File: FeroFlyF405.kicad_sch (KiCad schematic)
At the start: 4 parts

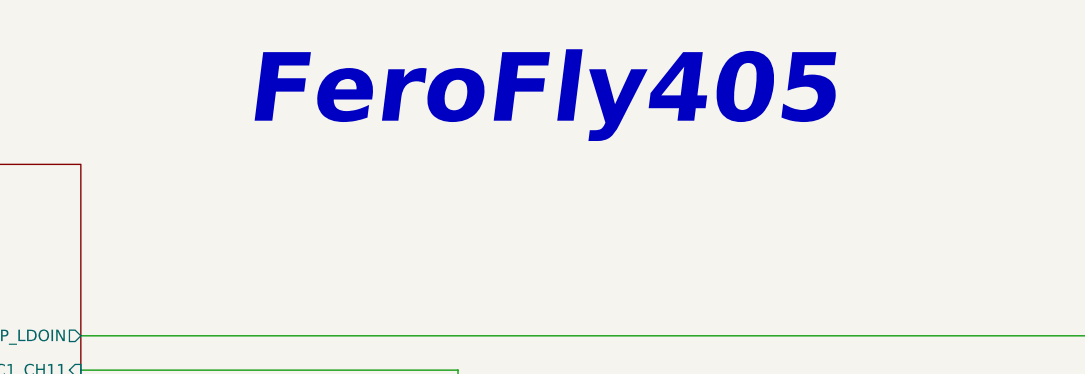
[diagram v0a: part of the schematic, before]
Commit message: refactor: change name from FeroFly405 to FeroFlyF405
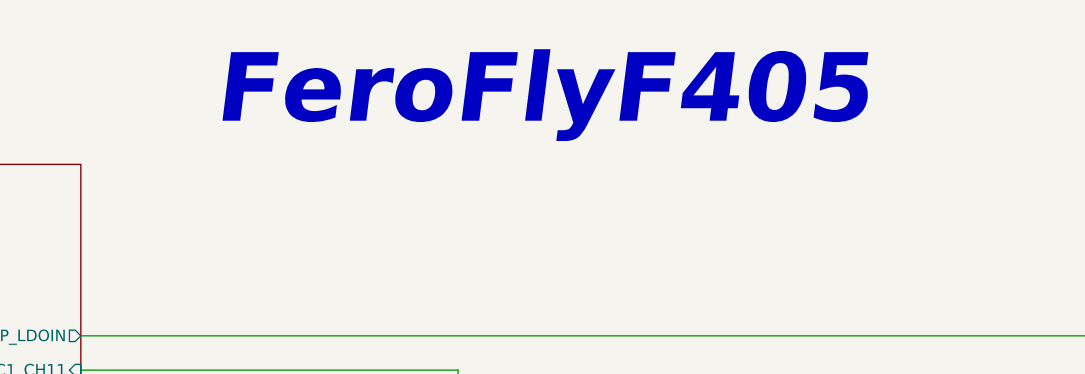
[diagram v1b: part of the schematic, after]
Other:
- note added: "FeroFlyF405"
- note removed: "FeroFly405"
- title: FeroFly405 -> FeroFlyF405
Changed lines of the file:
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@@
 	(paper "A4")
 	(title_block
-		(title "FeroFly405")
+		(title "FeroFlyF405")
 		(date "2026-07-22")
 		(rev "1")
-		(comment 3 "GitHub: https://github.com/Ozonised/FeroFly405")
+		(comment 3 "GitHub: https://github.com/Ozonised/FeroFlyF405")
 		(comment 4 "Designed by: Farhan Khan")
 	)
@@
 		)
 	)
-	(text "FeroFly405"
+	(text "FeroFlyF405"
 		(exclude_from_sim no)
 		(at 149.098 29.972 0)
@@
 		)
 		(instances
-			(project "FeroFly"
+			(project "FeroFlyF405"
 				(path "/8fea5468-8d8d-4bdb-afc0-e65b62c92669"
 					(reference "H103")
@@
 		)
 		(instances
-			(project "FeroFly"
+			(project "FeroFlyF405"
 				(path "/8fea5468-8d8d-4bdb-afc0-e65b62c92669"
 					(reference "H101")
@@
 		)
 		(instances
-			(project "FeroFly"
+			(project "FeroFlyF405"
 				(path "/8fea5468-8d8d-4bdb-afc0-e65b62c92669"
 					(reference "H104")
@@
 		)
 		(instances
-			(project "FeroFly"
+			(project "FeroFlyF405"
 				(path "/8fea5468-8d8d-4bdb-afc0-e65b62c92669"
 					(reference "H102")
@@
 		)
 		(instances
-			(project "FeroFly"
+			(project "FeroFlyF405"
 				(path "/8fea5468-8d8d-4bdb-afc0-e65b62c92669"
 					(page "4")
@@
 		)
 		(instances
-			(project "FeroFly"
+			(project "FeroFlyF405"
 				(path "/8fea5468-8d8d-4bdb-afc0-e65b62c92669"
 					(page "3")
@@
 		)
 		(instances
-			(project "FeroFly"
+			(project "FeroFlyF405"
 				(path "/8fea5468-8d8d-4bdb-afc0-e65b62c92669"
 					(page "2")
@@
 		)
 		(instances
-			(project "FeroFly"
+			(project "FeroFlyF405"
 				(path "/8fea5468-8d8d-4bdb-afc0-e65b62c92669"
 					(page "7")

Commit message: refactor(schematic): assign net classes and fix USB net label assingment
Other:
- sheet MCU ports: added SPI1_CS, SPI1_MISO, SPI1_MOSI, SPI1_SCK; removed D_SPI1_CS, D_SPI1_MISO, D_SPI1_MOSI, D_SPI1_SCK
- sheet Peripherals ports: added SPI1_CS, SPI1_MISO, SPI1_MOSI, SPI1_SCK; removed D_SPI1_CS, D_SPI1_MISO, D_SPI1_MOSI, D_SPI1_SCK
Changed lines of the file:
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@@
 			)
 		)
-		(pin "D_SPI1_CS" output
+		(pin "SPI1_CS" output
 			(at 99.06 110.49 0)
 			(effects
@@
 			)
 		)
-		(pin "D_SPI1_MISO" input
+		(pin "SPI1_MISO" input
 			(at 99.06 107.95 0)
 			(effects
@@
 			)
 		)
-		(pin "D_SPI1_MOSI" output
+		(pin "SPI1_MOSI" output
 			(at 99.06 105.41 0)
 			(effects
@@
 			)
 		)
-		(pin "D_SPI1_SCK" output
+		(pin "SPI1_SCK" output
 			(at 99.06 102.87 0)
 			(effects
@@
 			)
 		)
-		(pin "D_SPI1_CS" output
+		(pin "SPI1_CS" output
 			(at 118.11 110.49 180)
 			(effects
@@
 			)
 		)
-		(pin "D_SPI1_MISO" input
+		(pin "SPI1_MISO" input
 			(at 118.11 107.95 180)
 			(effects
@@
 			)
 		)
-		(pin "D_SPI1_MOSI" output
+		(pin "SPI1_MOSI" output
 			(at 118.11 105.41 180)
 			(effects
@@
 			)
 		)
-		(pin "D_SPI1_SCK" output
+		(pin "SPI1_SCK" output
 			(at 118.11 102.87 180)
 			(effects

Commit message: refactor: change motor output, renamed power nets
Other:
- sheet IO ports: added D_ADC1_CH10; removed D_ADC2_CH12
- sheet MCU ports: added D_ADC1_CH10, D_ADC2_CH13; removed D_ADC1_CH11, D_ADC2_CH12
- sheet Power ports: added D_ADC2_CH13; removed D_ADC1_CH11
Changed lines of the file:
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@@
 			)
 		)
-		(pin "D_ADC1_CH11" input
+		(pin "D_ADC2_CH13" input
 			(at 139.7 95.25 90)
 			(effects
@@
 			)
 		)
-		(pin "D_ADC2_CH12" input
+		(pin "D_ADC1_CH10" input
 			(at 184.15 97.79 0)
 			(effects
@@
 			)
 		)
-		(pin "D_ADC1_CH11" input
+		(pin "D_ADC2_CH13" input
 			(at 97.79 60.96 0)
 			(effects
@@
 			)
 		)
-		(pin "D_ADC2_CH12" input
+		(pin "D_ADC1_CH10" input
 			(at 199.39 97.79 180)
 			(effects
